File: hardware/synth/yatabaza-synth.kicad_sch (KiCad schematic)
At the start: 31 parts, among them P1 Φ, P2 BUS, P3 POWER, P4 AUDIO, U1 MCP23017, U2 YM3812, U3 74HC14, U4 YM3014B, U5 NE5532, Y1 3.58MHz

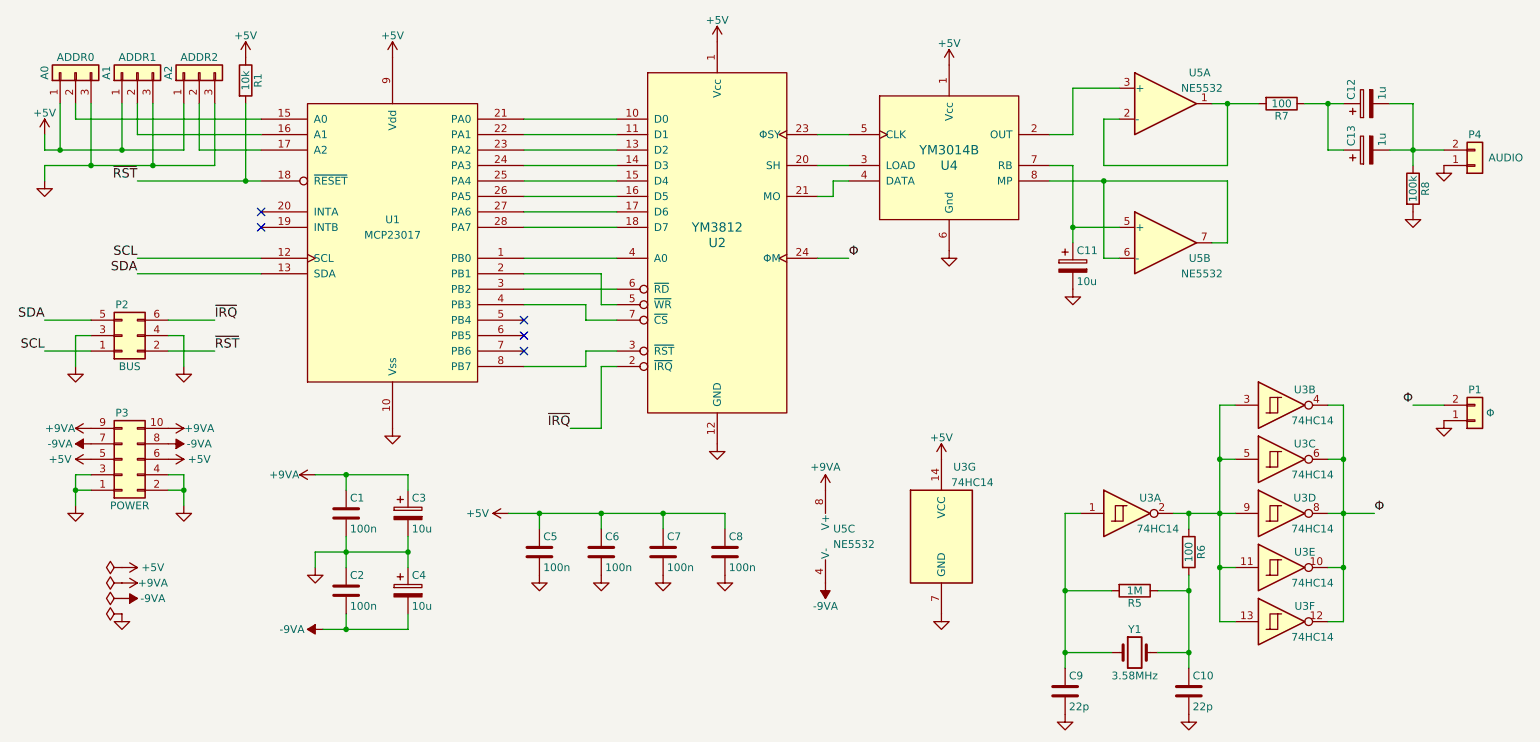
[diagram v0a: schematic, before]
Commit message: ~ Change resistors to US style.
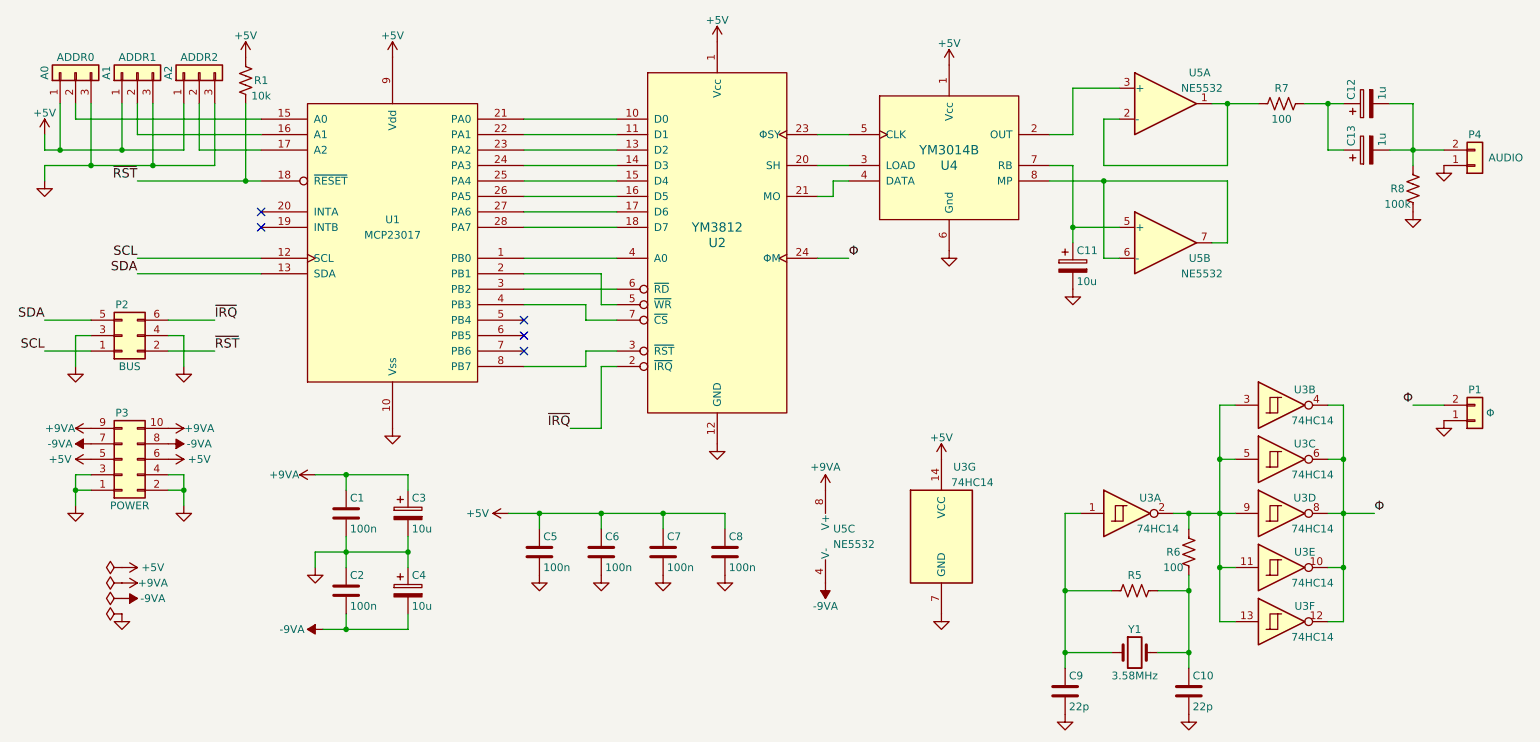
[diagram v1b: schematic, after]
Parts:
- R1, R6, R7, R8: symbol Device:R -> Device:R_US
- R5: value 1M -> (none); footprint Resistor_THT:R_Axial_DIN0204_L3.6mm_D1.6mm_P2.54mm_Vertical -> (none); symbol Device:R -> Device:R_US
- U1: footprint (none) -> Package_DIP:DIP-28_W7.62mm
- U2: footprint (none) -> Package_DIP:DIP-24_W15.24mm
- U4: footprint (none) -> Package_DIP:DIP-8_W7.62mm
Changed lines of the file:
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@@
       (effects (font (size 1.524 1.524)))
     )
-    (property "Footprint" "" (id 2) (at 182.88 59.69 0)
+    (property "Footprint" "Package_DIP:DIP-8_W7.62mm" (id 2) (at 182.88 59.69 0)
       (effects (font (size 1.524 1.524)) hide)
     )
@@
     (property "Reference" "U1" (id 0) (at 85.09 69.85 0))
     (property "Value" "MCP23017" (id 1) (at 85.09 72.39 0))
-    (property "Footprint" "" (id 2) (at 85.09 90.17 0)
+    (property "Footprint" "Package_DIP:DIP-28_W7.62mm" (id 2) (at 85.09 90.17 0)
       (effects (font (size 1.27 1.27)) hide)
     )
@@
     (pin "2")
   )
-  (symbol (lib_id "Device:R") (at 252.73 64.77 0) (unit 1)
-    (in_bom yes) (on_board yes)
-    (property "Reference" "R8" (id 0) (at 254.762 64.77 90))
-    (property "Value" "100k" (id 1) (at 252.73 64.77 90))
-    (property "Footprint" "Resistor_THT:R_Axial_DIN0204_L3.6mm_D1.6mm_P2.54mm_Vertical" (id 2) (at 250.952 64.77 90)
+  (symbol (lib_id "Device:R_US") (at 252.73 64.77 0) (unit 1)
+    (in_bom yes) (on_board yes)
+    (property "Reference" "R8" (id 0) (at 250.19 64.77 0))
+    (property "Value" "100k" (id 1) (at 250.19 67.31 0))
+    (property "Footprint" "Resistor_THT:R_Axial_DIN0204_L3.6mm_D1.6mm_P2.54mm_Vertical" (id 2) (at 253.746 65.024 90)
       (effects (font (size 1.27 1.27)) hide)
     )
@@
     (pin "2")
   )
-  (symbol (lib_id "Device:R") (at 231.14 50.8 270) (unit 1)
-    (in_bom yes) (on_board yes)
-    (property "Reference" "R7" (id 0) (at 231.14 52.832 90))
-    (property "Value" "100" (id 1) (at 231.14 50.8 90))
-    (property "Footprint" "Resistor_THT:R_Axial_DIN0204_L3.6mm_D1.6mm_P2.54mm_Vertical" (id 2) (at 231.14 49.022 90)
+  (symbol (lib_id "Device:R_US") (at 231.14 50.8 270) (unit 1)
+    (in_bom yes) (on_board yes)
+    (property "Reference" "R7" (id 0) (at 231.14 48.26 90))
+    (property "Value" "100" (id 1) (at 231.14 53.34 90))
+    (property "Footprint" "Resistor_THT:R_Axial_DIN0204_L3.6mm_D1.6mm_P2.54mm_Vertical" (id 2) (at 230.886 51.816 90)
       (effects (font (size 1.27 1.27)) hide)
     )
@@
     (pin "7")
   )
-  (symbol (lib_id "Device:R") (at 207.01 130.81 270) (unit 1)
-    (in_bom yes) (on_board yes)
-    (property "Reference" "R5" (id 0) (at 207.01 132.842 90))
-    (property "Value" "1M" (id 1) (at 207.01 130.81 90))
-    (property "Footprint" "Resistor_THT:R_Axial_DIN0204_L3.6mm_D1.6mm_P2.54mm_Vertical" (id 2) (at 207.01 129.032 90)
+  (symbol (lib_id "Device:R_US") (at 207.01 130.81 270) (unit 1)
+    (in_bom yes) (on_board yes)
+    (property "Reference" "R5" (id 0) (at 207.01 128.27 90))
+    (property "Value" "" (id 1) (at 207.01 133.35 90))
+    (property "Footprint" "" (id 2) (at 206.756 131.826 90)
       (effects (font (size 1.27 1.27)) hide)
     )
@@
     (pin "2")
   )
-  (symbol (lib_id "Device:R") (at 215.9 124.46 0) (unit 1)
-    (in_bom yes) (on_board yes)
-    (property "Reference" "R6" (id 0) (at 217.932 124.46 90))
-    (property "Value" "100" (id 1) (at 215.9 124.46 90))
-    (property "Footprint" "Resistor_THT:R_Axial_DIN0204_L3.6mm_D1.6mm_P2.54mm_Vertical" (id 2) (at 214.122 124.46 90)
+  (symbol (lib_id "Device:R_US") (at 215.9 124.46 0) (unit 1)
+    (in_bom yes) (on_board yes)
+    (property "Reference" "R6" (id 0) (at 213.36 124.46 0))
+    (property "Value" "100" (id 1) (at 213.36 127 0))
+    (property "Footprint" "Resistor_THT:R_Axial_DIN0204_L3.6mm_D1.6mm_P2.54mm_Vertical" (id 2) (at 216.916 124.714 90)
       (effects (font (size 1.27 1.27)) hide)
     )
@@
       (effects (font (size 1.524 1.524)))
     )
-    (property "Footprint" "" (id 2) (at 138.43 62.23 0)
+    (property "Footprint" "Package_DIP:DIP-24_W15.24mm" (id 2) (at 138.43 62.23 0)
       (effects (font (size 1.524 1.524)) hide)
     )
@@
     (pin "1")
   )
-  (symbol (lib_id "Device:R") (at 60.96 46.99 0) (unit 1)
-    (in_bom yes) (on_board yes)
-    (property "Reference" "R1" (id 0) (at 62.992 46.99 90))
-    (property "Value" "10k" (id 1) (at 60.96 46.99 90))
-    (property "Footprint" "Resistor_THT:R_Axial_DIN0204_L3.6mm_D1.6mm_P2.54mm_Vertical" (id 2) (at 59.182 46.99 90)
-      (effects (font (size 1.27 1.27)) hide)
-    )
+  (symbol (lib_id "Device:R_US") (at 60.96 46.99 0) (unit 1)
+    (in_bom yes) (on_board yes)
+    (property "Reference" "R1" (id 0) (at 63.5 46.99 0))
+    (property "Value" "10k" (id 1) (at 63.5 49.53 0))
+    (property "Footprint" "Resistor_THT:R_Axial_DIN0204_L3.6mm_D1.6mm_P2.54mm_Vertical" (id 2) (at 61.976 47.244 90)
+      (effects (font (size 1.27 1.27)) hide)
+    )
